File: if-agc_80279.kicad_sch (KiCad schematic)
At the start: 0 parts

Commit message: work on if-agc
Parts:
- added C79-1, C79-2: 200p, symbol Device:C_Small_US
- added C79-10, C79-7, C79-9: .01u, symbol Device:C_Small_US
- added C79-10, C79-5: 150p, symbol Device:C_Small_US
- added C79-11, C79-6: 430p, symbol Device:C_Small_US
- added C79-20, C79-3, C79-4, C79-8: .1u, symbol Device:C_Small_US
- added C79-21: 1m, symbol Device:C_Polarized_Small_US
- added D79-1, D79-2, D79-3: HP 5082-3379, symbol Device:D
- added D79-4, D79-5: 1N4154, symbol Device:D
- added L3, L5: L_Small, symbol Device:L_Small
- added L4, L6: L_Trim, symbol Device:L_Trim
- added Q79-1, Q79-2: MPS3693, symbol Transistor_BJT:Q_NPN_EBC
- added R79-1, R79-5: 22k, symbol Device:R_Small_US
- added R79-17, R79-18, R79-19: 1k, symbol Device:R_Small_US
- added R79-2: 2.2k, symbol Device:R_Small_US
- added R79-20: 10k, symbol Device:R_Potentiometer_Trim_US
- added R79-3, R79-7: 220, symbol Device:R_Small_US
- added R79-4, R79-8: 100, symbol Device:R_Small_US
- added R79-6: 4.7k, symbol Device:R_Small_US
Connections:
- new net: C79-5.1, L4.2
- new net: C79-5.2, C79-6.1, C79-7.1, Q79-2.2 (B), R79-5.2, R79-6.1
- new net: C79-2.1, Q79-1.2 (B), R79-1.2, R79-2.1
- new net: C79-2.2, D79-1.2 (A)
- new net: R79-1.1, R79-5.1
- new net: C79-9.1, Q79-2.1 (E), R79-7.1
- new net: C79-1.2, R79-19.1
- new net: C79-7.2, D79-2.2 (A), R79-18.1
- new net: C79-20.1, D79-5.1 (K), R79-17.2, R79-18.2, R79-19.2
- new net: C79-8.1, L5.1, R79-8.2
- new net: C79-3.1, Q79-1.1 (E), R79-3.1
- new net: L3.2, Q79-1.3 (C)
- new net: C79-10.2, C79-11.1
- new net: C79-4.1, L3.1, R79-4.2
- new net: D79-5.2 (A), R79-20.3
- new net: C79-10.1, L5.2, Q79-2.3 (C)
- new net: C79-10.2, D79-3.2 (A), R79-17.1
- new net: D79-4.2 (A), R79-20.1, R79-20.2
- new net: C79-10.1, L6.2
- new net +12: R79-4.1, R79-8.1
- new net AUDIO: C79-21.2
- new net GND: C79-11.2, C79-20.2, C79-3.2, C79-4.2, C79-6.2, C79-8.2, C79-9.2, D79-1.1 (K), D79-2.1 (K), D79-3.1 (K), L4.1, L6.1, R79-2.2, R79-3.2, R79-6.2, R79-7.2
- new net IN: C79-1.1
- new net S MTR: D79-4.1 (K)
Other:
- note added: "T1"
- note added: "T2"

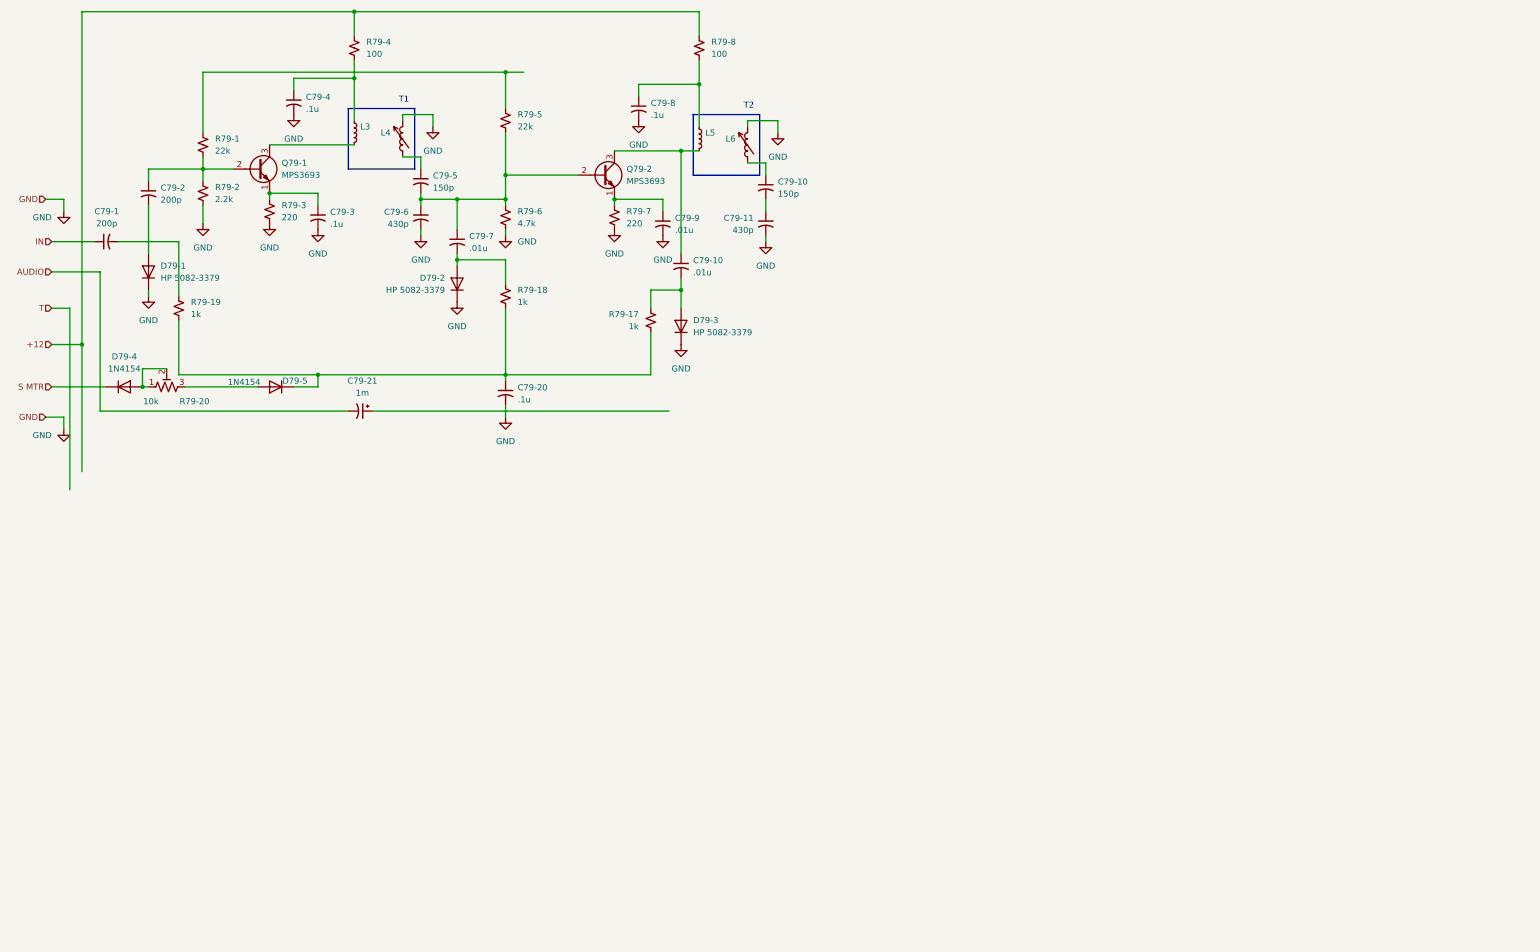
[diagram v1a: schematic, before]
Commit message: Complete IF-AGC schematic and SPICE models
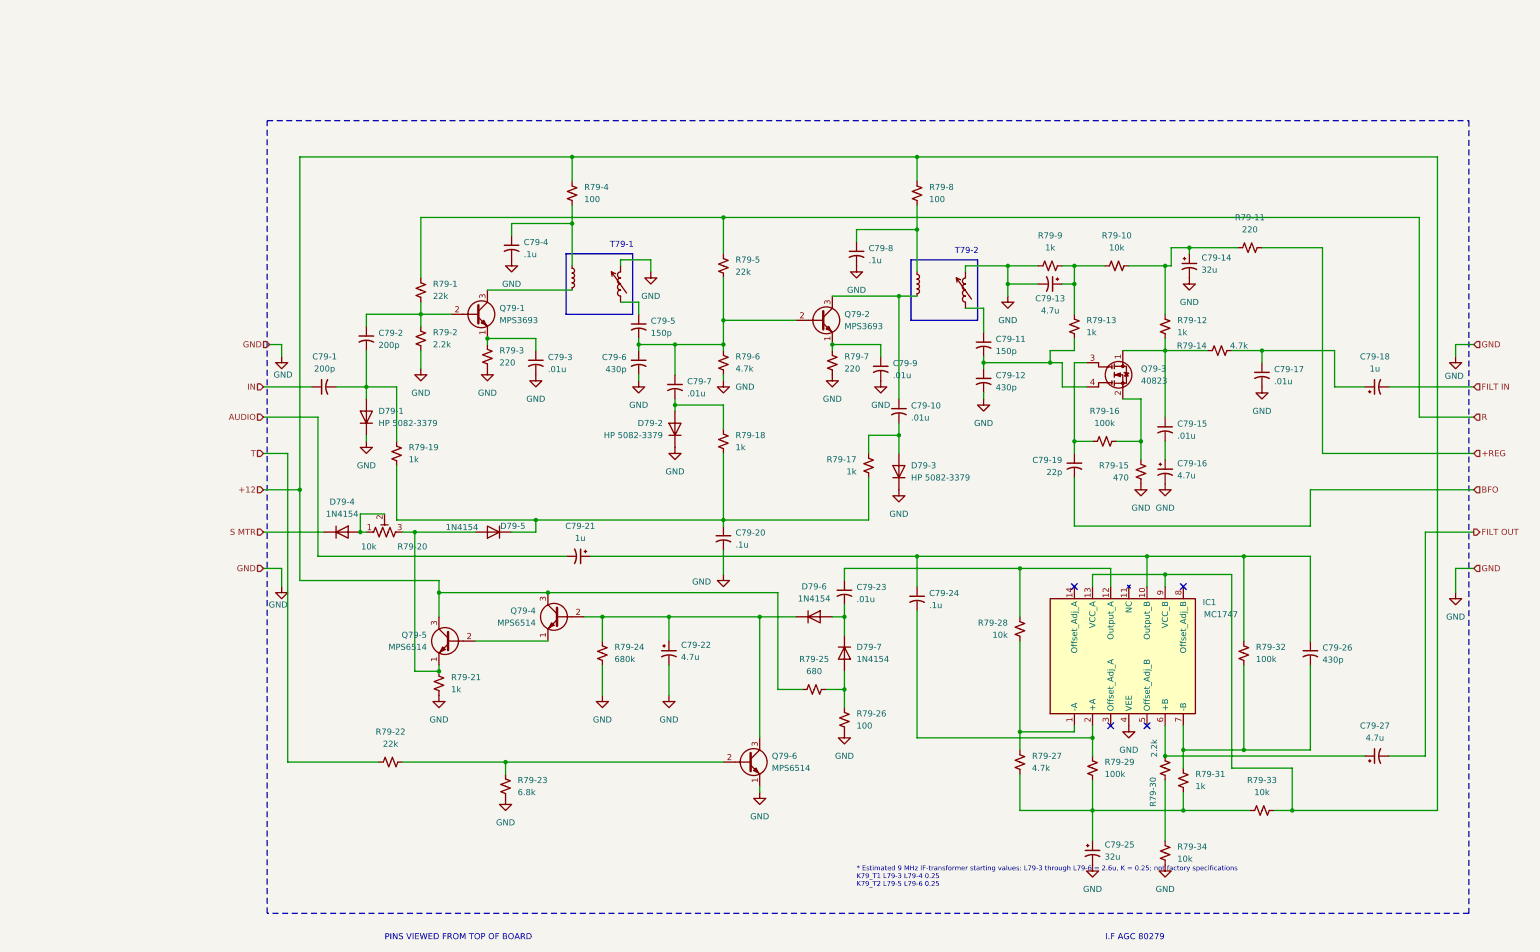
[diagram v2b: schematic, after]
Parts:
- added C79-13, C79-16, C79-22, C79-27: 4.7u, symbol Device:C_Polarized_Small_US
- added C79-14, C79-25: 32u, symbol Device:C_Polarized_Small_US
- added C79-15, C79-17, C79-23: .01u, symbol Device:C_Small_US
- added C79-18: 1u, symbol Device:C_Polarized_Small_US
- added C79-19: 22p, symbol Device:C_Small_US
- added C79-24: .1u, symbol Device:C_Small_US
- added C79-26: 430p, symbol Device:C_Small_US
- added D79-6, D79-7: 1N4154, symbol Device:D
- added IC1: MC1747, symbol triton_iv:MC1747
- added Q79-3: 40823, Package_TO_SOT_THT:TO-72-4, symbol triton_iv:40823
- added Q79-4, Q79-5, Q79-6: MPS6514, symbol Transistor_BJT:Q_NPN_EBC
- added R79-10, R79-28, R79-33, R79-34: 10k, symbol Device:R_Small_US
- added R79-11: 220, symbol Device:R_Small_US
- added R79-12, R79-13, R79-21, R79-31, R79-9: 1k, symbol Device:R_Small_US
- added R79-14, R79-27: 4.7k, symbol Device:R_Small_US
- added R79-15: 470, symbol Device:R_Small_US
- added R79-16, R79-29, R79-32: 100k, symbol Device:R_Small_US
- added R79-22: 22k, symbol Device:R_Small_US
- added R79-23: 6.8k, symbol Device:R_Small_US
- added R79-24: 680k, symbol Device:R_Small_US
- added R79-25: 680, symbol Device:R_Small_US
- added R79-26: 100, symbol Device:R_Small_US
- added R79-30: 2.2k, symbol Device:R_Small_US
- C79-21: value 1m -> 1u
- C79-3: value .1u -> .01u
- L79-3: renamed from L3; value L_Small -> 2.6u
- L79-4: renamed from L4; value L_Trim -> 2.6u
- L79-5: renamed from L5; value L_Small -> 2.6u
- L79-6: renamed from L6; value L_Trim -> 2.6u
- renumbered C79-10 to C79-11, C79-11 to C79-12
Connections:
- net +12: now also IC1.13 (VCC_A), IC1.9 (VCC_B), Q79-4.3 (C), Q79-5.3 (C), R79-25.1, R79-33.2
- net GND: now also C79-13.2, C79-14.2, C79-16.2, C79-17.2, C79-22.2, C79-25.2, IC1.4 (VEE), Q79-6.1 (E), R79-15.2, R79-21.2, R79-23.2, R79-24.2, R79-26.2, R79-34.2, R79-9.1
- net T: now also R79-22.1
- net at C79-2.2, D79-1.2 (A): now also C79-1.2, R79-19.1
- net R: now reaches R79-1.1, R79-5.1
- net at C79-11.2, C79-12.1: now also Q79-3.4 (S), R79-13.2
- net at C79-21.1: now also C79-24.1, C79-26.1, IC1.10 (Output_B), R79-32.1
- net at D79-5.2 (A), R79-20.3: now also Q79-5.1 (E), R79-21.1
- new net: C79-26.2, IC1.7 (-B), R79-31.1, R79-32.2
- new net: C79-27.1, IC1.6 (+B), R79-30.1
- new net: Q79-6.2 (B), R79-22.2, R79-23.1
- new net: C79-22.1, D79-6.1 (K), Q79-4.2 (B), Q79-6.3 (C), R79-24.1
- new net: R79-30.2, R79-34.1
- new net: D79-7.2 (A), R79-25.2, R79-26.1
- new net: C79-14.1, R79-10.2, R79-11.1, R79-12.1
- new net: C79-13.1, R79-10.1, R79-13.1, R79-9.2
- new net: C79-17.1, C79-18.1, R79-14.2
- new net: C79-23.2, D79-6.2 (A), D79-7.1 (K)
- new net: C79-15.2, C79-16.1
- new net: Q79-4.1 (E), Q79-5.2 (B)
- new net: C79-24.2, IC1.2 (+A), R79-29.1
- new net: IC1.1 (-A), R79-27.1, R79-28.2
- new net: C79-23.1, IC1.12 (Output_A), R79-28.1
- new net: C79-15.1, Q79-3.1 (D), R79-12.2, R79-14.1
- new net: C79-19.1, Q79-3.3 (G1), R79-16.1
- new net: Q79-3.2 (G2), R79-15.1, R79-16.2
- new net: C79-25.1, R79-27.2, R79-29.2, R79-31.2, R79-33.1
- new net +REG: R79-11.2
- new net BFO: C79-19.2
- new net FILT IN: C79-18.2
- new net FILT OUT: C79-27.2
- no-connect marks 0 -> 4
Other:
- note added: "* Estimated 9 MHz IF-transformer starting values: L79-3 through L79-6 = 2.6u, K = 0.25; not factory specifications K79_T1 L79-3 L79-4 0.25 K79_T2 L79-5 L79-6 0.25"
- note added: "I.F AGC 80279"
- note added: "PINS VIEWED FROM TOP OF BOARD"
- note added: "T79-1"
- note added: "T79-2"
- note removed: "T1"
- note removed: "T2"
- company: Andy McCann KA3KAF & DOug McCann KA3KAG -> Andy McCann KA3KAF & Doug McCann KA3KAG
- title: (none) -> IF-AGC 80279
- moved on the sheet: C79-1, C79-10, C79-11, C79-12, C79-2, C79-20, C79-21, C79-3, C79-4, C79-5, C79-6, C79-7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

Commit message: sims 1-3 run on ig-agc
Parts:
- added I79-SIM1: 0, symbol Simulation_SPICE:VDC
- added R79-SIM1: 25k, symbol Device:R_Small_US
- added R79-SIM2: 1k, symbol Device:R_Small_US
- added V79-SIM1: 13.8, symbol Simulation_SPICE:VDC
- added V79-SIM2: 8.0, symbol Simulation_SPICE:VDC
- added V79-SIM3: 12.1, symbol Simulation_SPICE:VDC
- added V79-SIM4: 0.2, symbol Simulation_SPICE:VDC
- added V79-SIM5: IF 1mV, symbol Simulation_SPICE:VSIN
- added V79-SIM6: 100m est., symbol Simulation_SPICE:VSIN
- L79-3, L79-4, L79-5, L79-6: value 2.6u -> 2.63u
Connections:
- net FILT OUT is gone; now on net FILT IN: C79-27.2
- net +12: now also V79-SIM1.1
- net +REG: now also V79-SIM2.1
- net AUDIO: now also R79-SIM1.1
- net BFO: now also V79-SIM6.1
- net GND: now also I79-SIM1.1, R79-SIM1.2, R79-SIM2.2, V79-SIM1.2, V79-SIM2.2, V79-SIM3.2, V79-SIM4.2, V79-SIM5.2, V79-SIM6.2
- net IN: now also V79-SIM5.1
- net R: now also V79-SIM3.1
- net S MTR: now also R79-SIM2.1
- net T: now also V79-SIM4.1
- net at R79-30.2, R79-34.1: now also C79-25.1, R79-27.2, R79-29.2, R79-31.2, R79-33.1
- net PIN_BIAS: now reaches C79-20.1, D79-5.1 (K), R79-17.2, R79-18.2, R79-19.2
- net PIN_BIAS: now also I79-SIM1.2
- net at C79-15.2, C79-16.1: now also Q79-3.4 (S), R79-15.1, R79-16.2
- net at C79-11.2, C79-12.1, R79-13.2: now also Q79-3.3 (G1); no longer Q79-3.4 (S)
- net at C79-19.1, R79-16.1: now also Q79-3.2 (G2); no longer Q79-3.3 (G1)
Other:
- note added: "* Estimated 9 MHz IF-transformer aligned values: L79-3 through L79-6 = 2.63u, K = 0.25; not factory specifications K79_T1 L79-3 L79-4 0.25 K79_T2 L79-5 L79-6 0.25"
- note added: ".options rshunt=1e12"
- note added: "SIMULATION ONLY — RECEIVE / NO-SIGNAL FIXTURE Sources are not part of the original 80279 assembly. BFO RF amplitude is estimated. PIN_BIAS current source is disabled except for Simulation 3."
- note removed: "* Estimated 9 MHz IF-transformer starting values: L79-3 through L79-6 = 2.6u, K = 0.25; not factory specifications K79_T1 L79-3 L79-4 0.25 K79_T2 L79-5 L79-6 0.25"
- moved on the sheet: C79-1, C79-10, C79-11, C79-12, C79-13, C79-14, C79-15, C79-16, C79-17, C79-18, C79-19, C79-2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
